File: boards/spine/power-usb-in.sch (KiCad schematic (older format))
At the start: 21 parts

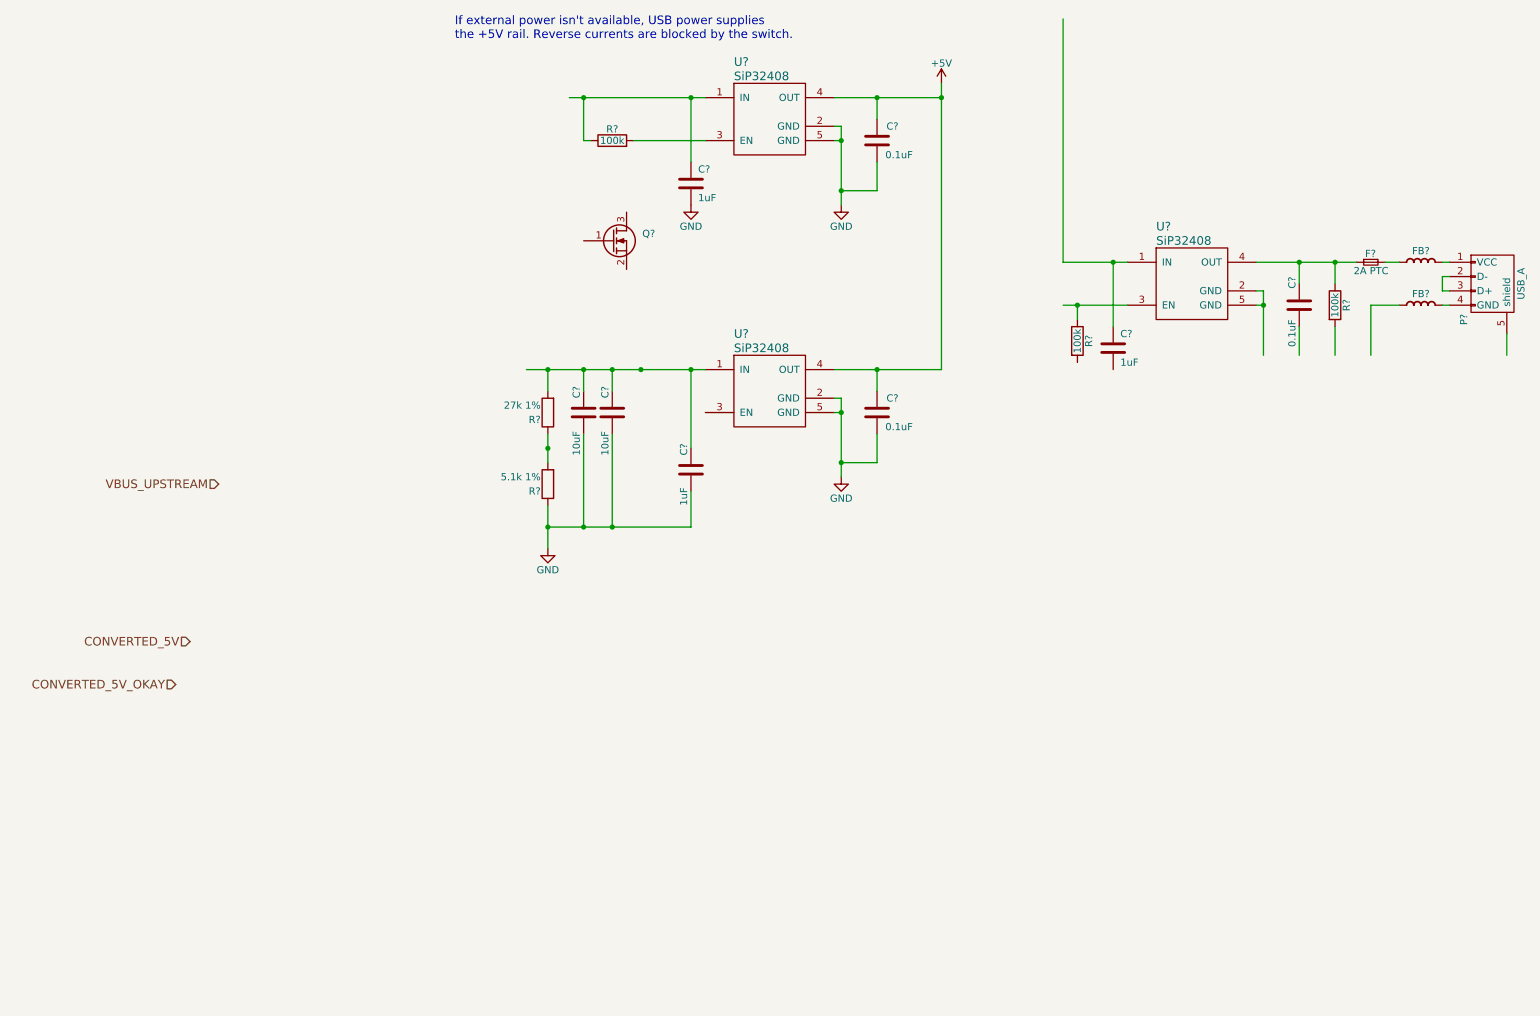
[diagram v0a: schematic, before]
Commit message: Power source switching
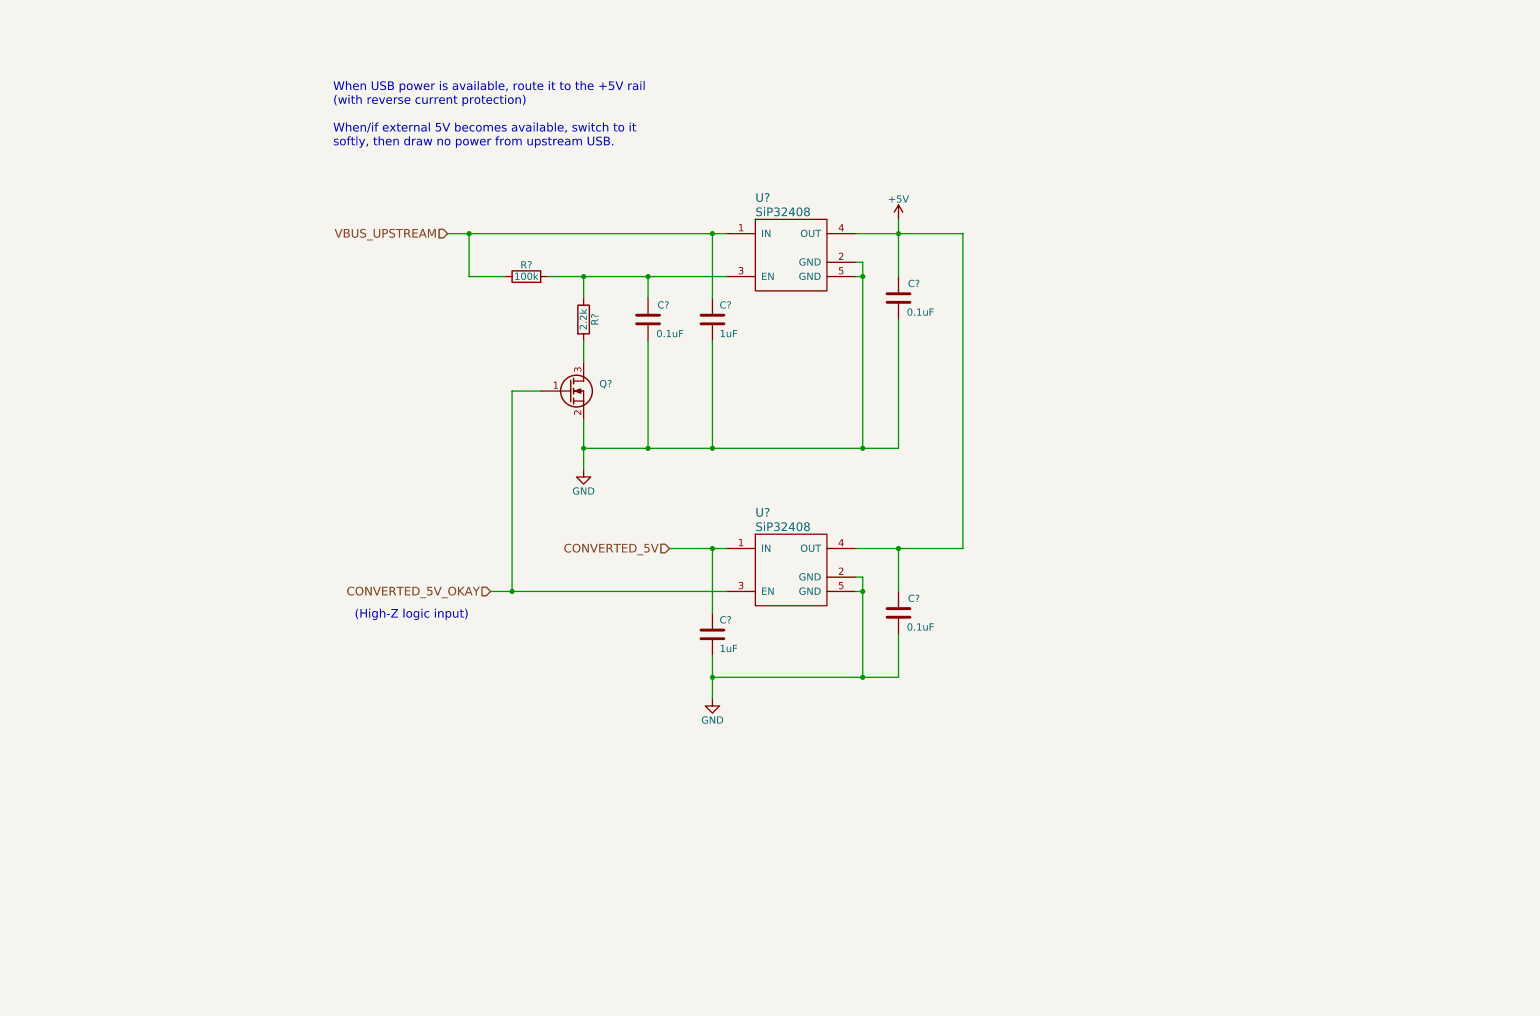
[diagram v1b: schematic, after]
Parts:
- removed C? (x2): 0.1uF, 0805, symbol C
- removed C? (x2): 1uF, 0805, symbol C
- removed C? (x2): 10uF, 1206, symbol C
- removed F?: 2A PTC, 1812, symbol F_Small
- removed FB? (x2): Ferrite bead, symbol FERRITE_BEAD
- removed P?: USB_A, symbol USB_A
- removed R? (x2): 100k, symbol R
- removed R?: 5.1k 1%, 0805, symbol R
- removed R?: 27k 1%, 0805, symbol R
- removed U? (x2): SiP32408, symbol SiP32408
- added C? (x2): 0.1uF, 0805, symbol C
- added C?: 1uF, 0805, symbol C
- added R?: 2.2k, symbol R
- added U?: SiP32408, symbol SiP32408
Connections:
- wire segments 76 -> 49
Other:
- note added: "(High-Z logic input)"
- note added: "When USB power is available, route it to the +5V rail\n(with reverse current protection)\n\nWhen/if external 5V becomes available, switch to it\nsoftly, then draw no power from upstream USB."
- note removed: "If external power isn't available, USB power supplies\nthe +5V rail. Reverse currents are blocked by the switch."
- moved on the sheet: C?, Q?, R?, U?

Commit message: Power management and such
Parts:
- removed U? (x2): SiP32408, symbol SiP32408
- added C70, C71: 10uF, 1206, symbol C
- added D7: 8.5VWM, symbol D_Schottky_x2_ACom_KKA
- added U11, U12: SiP32408, symbol SiP32408
- gave numbers to parts that had none: 8
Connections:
- net +5V: now also C70.1, C71.1, D7.1 (K), D7.2 (K), U11.4 (OUT), U12.4 (OUT)
- net CONVERTED_5V: now also U12.1 (IN)
- net CONVERTED_5V_OKAY: now also U12.3 (EN)
- net GND: now also C70.2, C71.2, D7.3 (A), U11.2 (GND), U11.5 (GND), U12.2 (GND), U12.5 (GND)
- net VBUS_UPSTREAM: now also U11.1 (IN)
- net at C65.2, R31.2, R32.1: now also U11.3 (EN)
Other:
- note added: "Transient clamping"
- moved on the sheet: C65, C66, C67, C68, C69, Q3, R31, R32

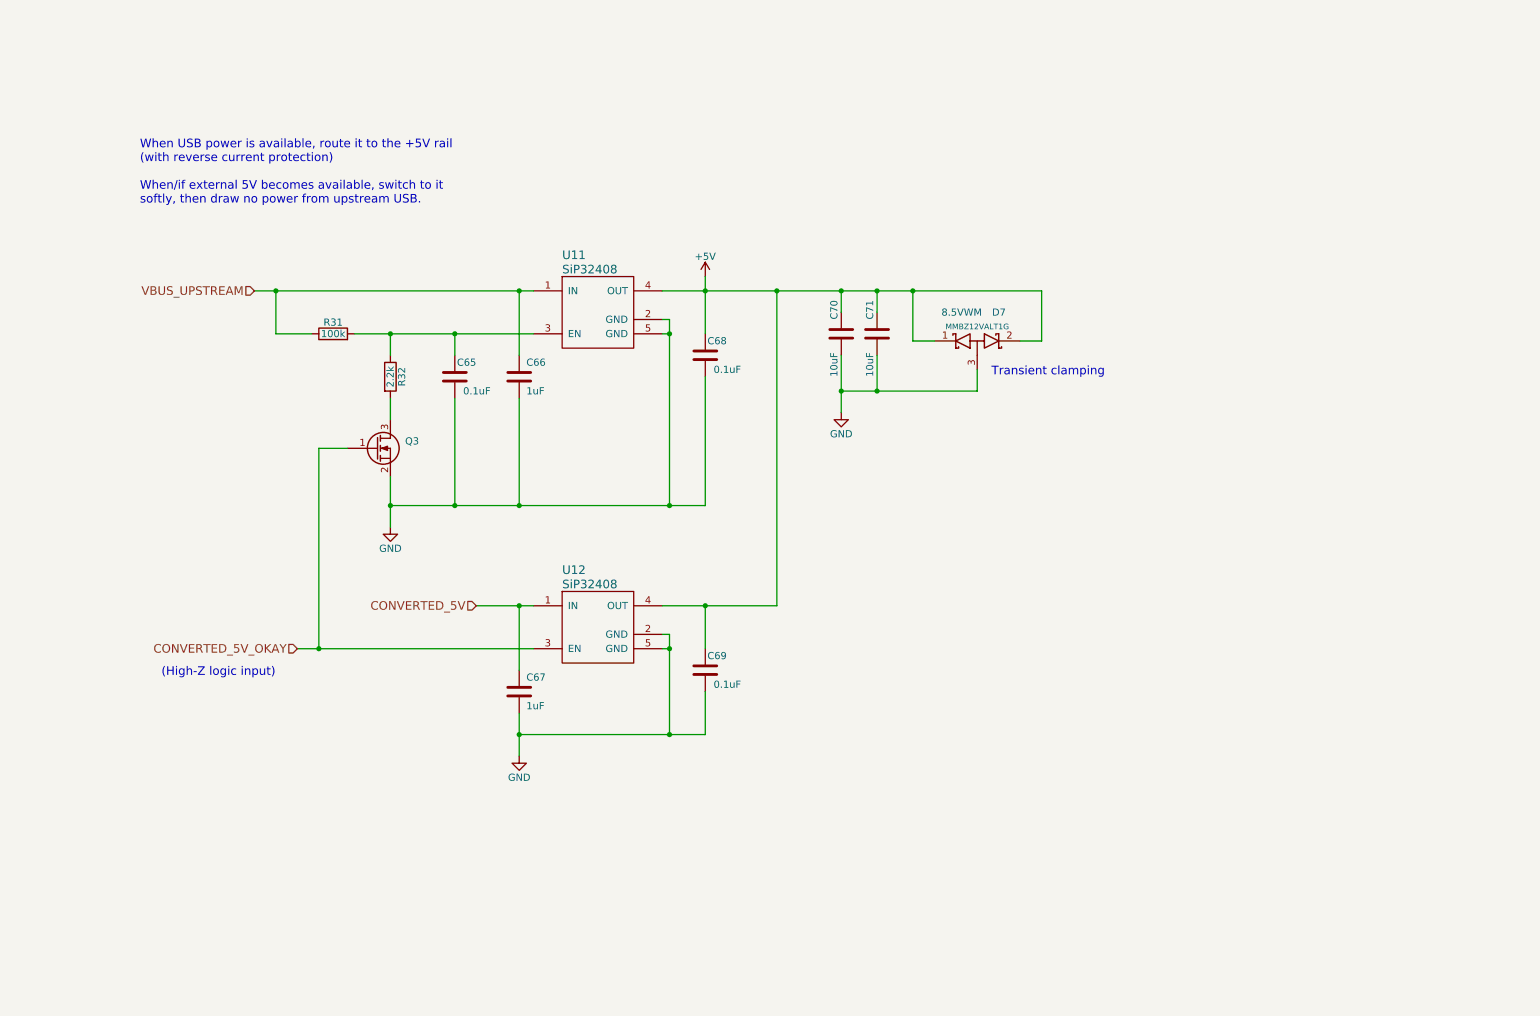
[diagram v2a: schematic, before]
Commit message: Clock generator, sync connectors, title blocks
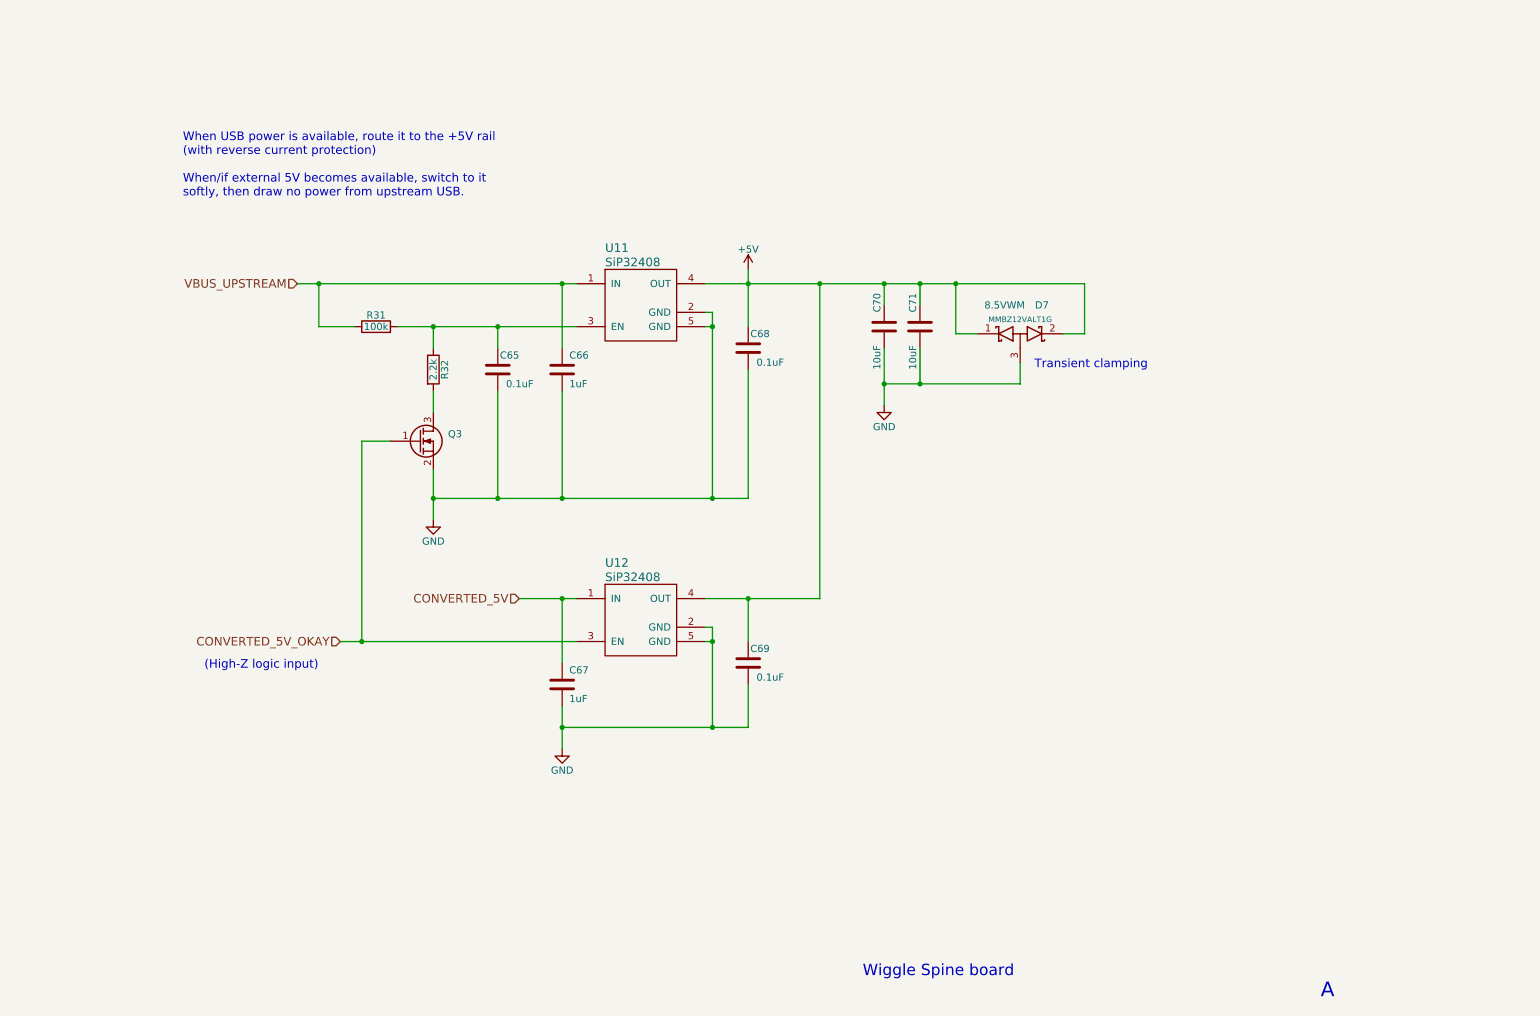
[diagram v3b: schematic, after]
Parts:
- C65, C66, C67, C68, C69: footprint 0805 -> Capacitors_SMD:C_0805
- C70, C71: footprint 1206 -> Capacitors_SMD:C_1206
- R31, R32: footprint (none) -> Resistors_SMD:R_0805
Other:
- note added: "A"
- note added: "Wiggle Spine board"
- moved on the sheet: C65, C66, C67, C68, C69, C70, C71, D7, Q3, R31, R32, U11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

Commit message: Schematic footprint and refdes work
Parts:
- D7, Q3: footprint (none) -> TO_SOT_Packages_SMD:SOT-23
- U11, U12: footprint (none) -> TDFN4:TDFN4
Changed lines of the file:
@@
 F 0 "Q3" H 3900 4050 50  0000 R CNN
 F 1 "IRFML8244" H 4200 3950 50  0001 R CNN
-F 2 "" H 3800 4100 29  0001 C CNN
+F 2 "TO_SOT_Packages_SMD:SOT-23" H 3800 4100 29  0001 C CNN
 F 3 "http://www.irf.com/product-info/datasheets/data/irfml8244pbf.pdf" H 3600 4000 60  0001 C CNN
 F 4 "Infineon" H 3600 4000 60  0001 C CNN "MfrId"
@@
 $EndComp
 $Comp
-L +5V #PWR0135
+L +5V #PWR137
 U 1 1 564D4EA6
 P 5900 2800
-F 0 "#PWR0135" H 5900 2650 50  0001 C CNN
+F 0 "#PWR137" H 5900 2650 50  0001 C CNN
 F 1 "+5V" H 5900 2940 50  0000 C CNN
 F 2 "" H 5900 2800 60  0000 C CNN
@@
 CONVERTED_5V_OKAY
 $Comp
-L GND #PWR0136
+L GND #PWR135
 U 1 1 564D0835
 P 3700 4550
-F 0 "#PWR0136" H 3700 4300 50  0001 C CNN
+F 0 "#PWR135" H 3700 4300 50  0001 C CNN
 F 1 "GND" H 3700 4400 50  0000 C CNN
 F 2 "" H 3700 4550 60  0000 C CNN
@@
 $EndComp
 $Comp
-L GND #PWR0137
+L GND #PWR136
 U 1 1 564D1BDA
 P 4600 6150
-F 0 "#PWR0137" H 4600 5900 50  0001 C CNN
+F 0 "#PWR136" H 4600 5900 50  0001 C CNN
 F 1 "GND" H 4600 6000 50  0000 C CNN
 F 2 "" H 4600 6150 60  0000 C CNN
@@
 F 0 "U11" H 4900 3250 60  0000 L CNN
 F 1 "SiP32408" H 4900 3150 60  0000 L CNN
-F 2 "" H 5200 3150 60  0001 C CNN
+F 2 "TDFN4:TDFN4" H 5200 3150 60  0001 C CNN
 F 3 "http://www.vishay.com/docs/63717/sip32408.pdf" H 5200 3150 60  0001 C CNN
 F 4 "Digikey" H 5150 2950 60  0001 C CNN "Vend1"
@@
 F 0 "U12" H 4900 5450 60  0000 L CNN
 F 1 "SiP32408" H 4900 5350 60  0000 L CNN
-F 2 "" H 5200 5350 60  0001 C CNN
+F 2 "TDFN4:TDFN4" H 5200 5350 60  0001 C CNN
 F 3 "http://www.vishay.com/docs/63717/sip32408.pdf" H 5200 5350 60  0001 C CNN
 F 4 "Digikey" H 5150 5150 60  0001 C CNN "Vend1"
@@
 $EndComp
 $Comp
-L GND #PWR0138
+L GND #PWR138
 U 1 1 564EBB09
 P 6850 3750
-F 0 "#PWR0138" H 6850 3500 50  0001 C CNN
+F 0 "#PWR138" H 6850 3500 50  0001 C CNN
 F 1 "GND" H 6850 3600 50  0000 C CNN
 F 2 "" H 6850 3750 60  0000 C CNN
@@
 F 0 "D7" H 8000 3450 50  0000 R CNN
 F 1 "8.5VWM" H 7550 3450 50  0000 L CNN
-F 2 "" H 7800 3250 60  0001 C CNN
+F 2 "TO_SOT_Packages_SMD:SOT-23" H 7800 3250 60  0001 C CNN
 F 3 "http://www.onsemi.com/pub_link/Collateral/MMBZ5V6ALT1-D.PDF" H 7800 3250 60  0001 C CNN
 F 4 "ON Semi" H 7450 3400 39  0001 L BNN "MfrId"
